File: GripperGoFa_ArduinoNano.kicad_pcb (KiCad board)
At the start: 2 copper layers, 52 x 45 mm, 19 parts, among them J1 Conn_01x02, J2 Conn_01x04, J3 Conn_01x03, J4 Conn_01x05, J5 Conn_01x02, U1 HCPL-2631, U2 HCPL-2631

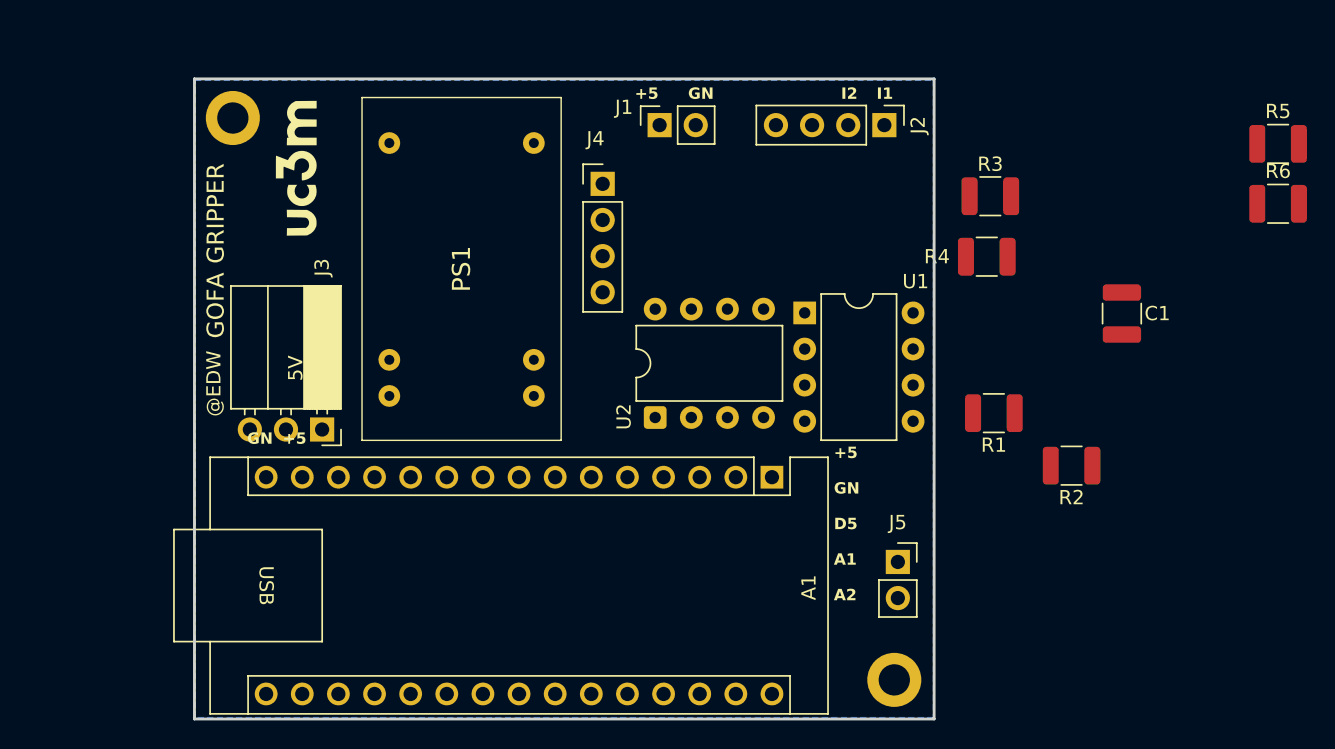
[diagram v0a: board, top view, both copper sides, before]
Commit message: update components
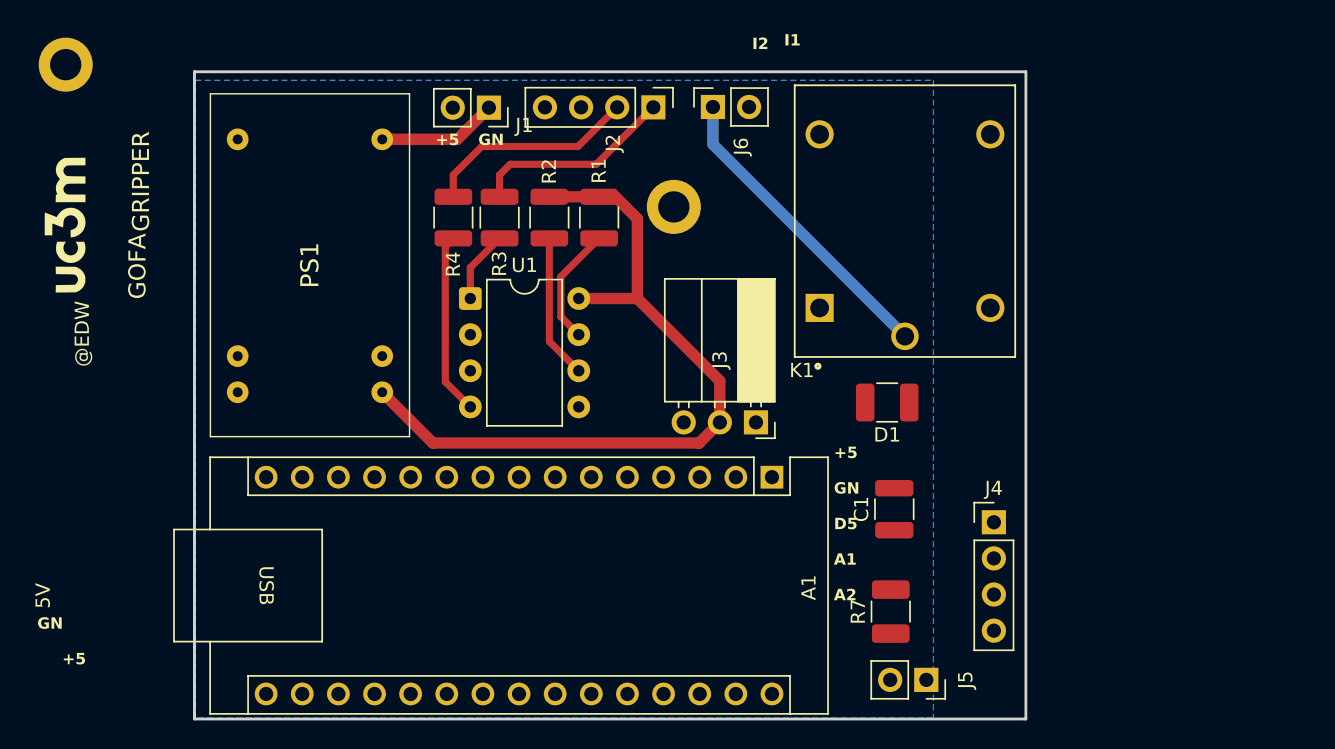
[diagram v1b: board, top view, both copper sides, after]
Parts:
- removed R5, R6: 2k7, Resistor_SMD:R_1210_3225Metric
- removed U2: HCPL-2631, Package_DIP:DIP-8_W7.62mm
- added D1: D, Resistor_SMD:R_1210_3225Metric_Pad1.30x2.65mm_HandSolder, F.Cu at (137.8, 96.2)
- added J6: Magnet, Connector_PinSocket_2.54mm:PinSocket_1x02_P2.54mm_Vertical, F.Cu at (125.5, 75.5)
- added K1: SRD-05VDC-SL-C, Relay_THT:RELAY_SRD-05VDC-SL-C, F.Cu at (139.0, 83.5)
- added R7: R, Resistor_SMD:R_1210_3225Metric_Pad1.30x2.65mm_HandSolder, F.Cu at (138.0, 111.0)
- J1: value Conn_01x02 -> VCC
- J2: value Conn_01x04 -> Input
- J3: value Conn_01x03 -> Servo
- J4: value Conn_01x05 -> OptSensor
- J5: value Conn_01x02 -> FSR
- moved R2 40.6 mm to (114.0, 83.2), turned to -90 degrees
- moved R4 37.6 mm to (107.2, 83.2), turned to -90 degrees
- moved H2 36.7 mm to (122.8, 82.5)
- moved J4 36.4 mm to (145.2, 104.7)
- moved R3 34.5 mm to (110.5, 83.2), turned to -90 degrees
- moved R1 31.0 mm to (117.5, 83.2), turned to -90 degrees
- moved J3 30.5 mm to (128.5, 97.7)
- moved U1 23.5 mm to (108.4, 88.9)
- moved C1 21.1 mm to (138.2, 103.8), turned to 90 degrees
- moved G 16.7 mm to (80.0, 83.8)
- moved J2 16.3 mm to (121.3, 75.5)
- moved H2 12.3 mm to (80.0, 72.5)
- moved J1 12.1 mm to (109.8, 75.5), turned to -90 degrees
- moved PS1 10.7 mm to (92.1, 77.8)
- moved J5 8.53 mm to (140.5, 115.8), turned to -90 degrees
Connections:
- A1 pad 10: /D7 -> /MagnetDO
- A1 pad 9: /D6 -> unconnected-(A1-D6-Pad9)
- J2 pad 3: Net-(J2-Pin_3) -> unconnected-(J2-Pin_3-Pad3)
- J2 pad 4: Net-(J2-Pin_4) -> unconnected-(J2-Pin_4-Pad4)
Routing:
- net +5V: track 0.00 -> 53.5 mm
- net Net-(J6-Pin_1): track 0.00 -> 21.7 mm
- net Net-(J2-Pin_2): track 0.00 -> 15.0 mm
- net Net-(J2-Pin_1): track 0.00 -> 14.3 mm
- net Net-(U1-A2): track 0.00 -> 12.8 mm
- net /DI2: track 0.05 -> 10.2 mm
- net +24V: track 0.00 -> 8.42 mm
- net /DI1: track 0.00 -> 8.40 mm
- net Net-(U1-A1): track 0.00 -> 5.08 mm
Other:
- board size 52 x 45 mm -> 58.5 x 45.5 mm
